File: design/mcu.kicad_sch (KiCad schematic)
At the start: 30 parts, among them J2 SWD_01X04, J3 DEBUG_SPI, U6 STM32H750VBTx, X1 ASTX-H11-25.000MHZ-T

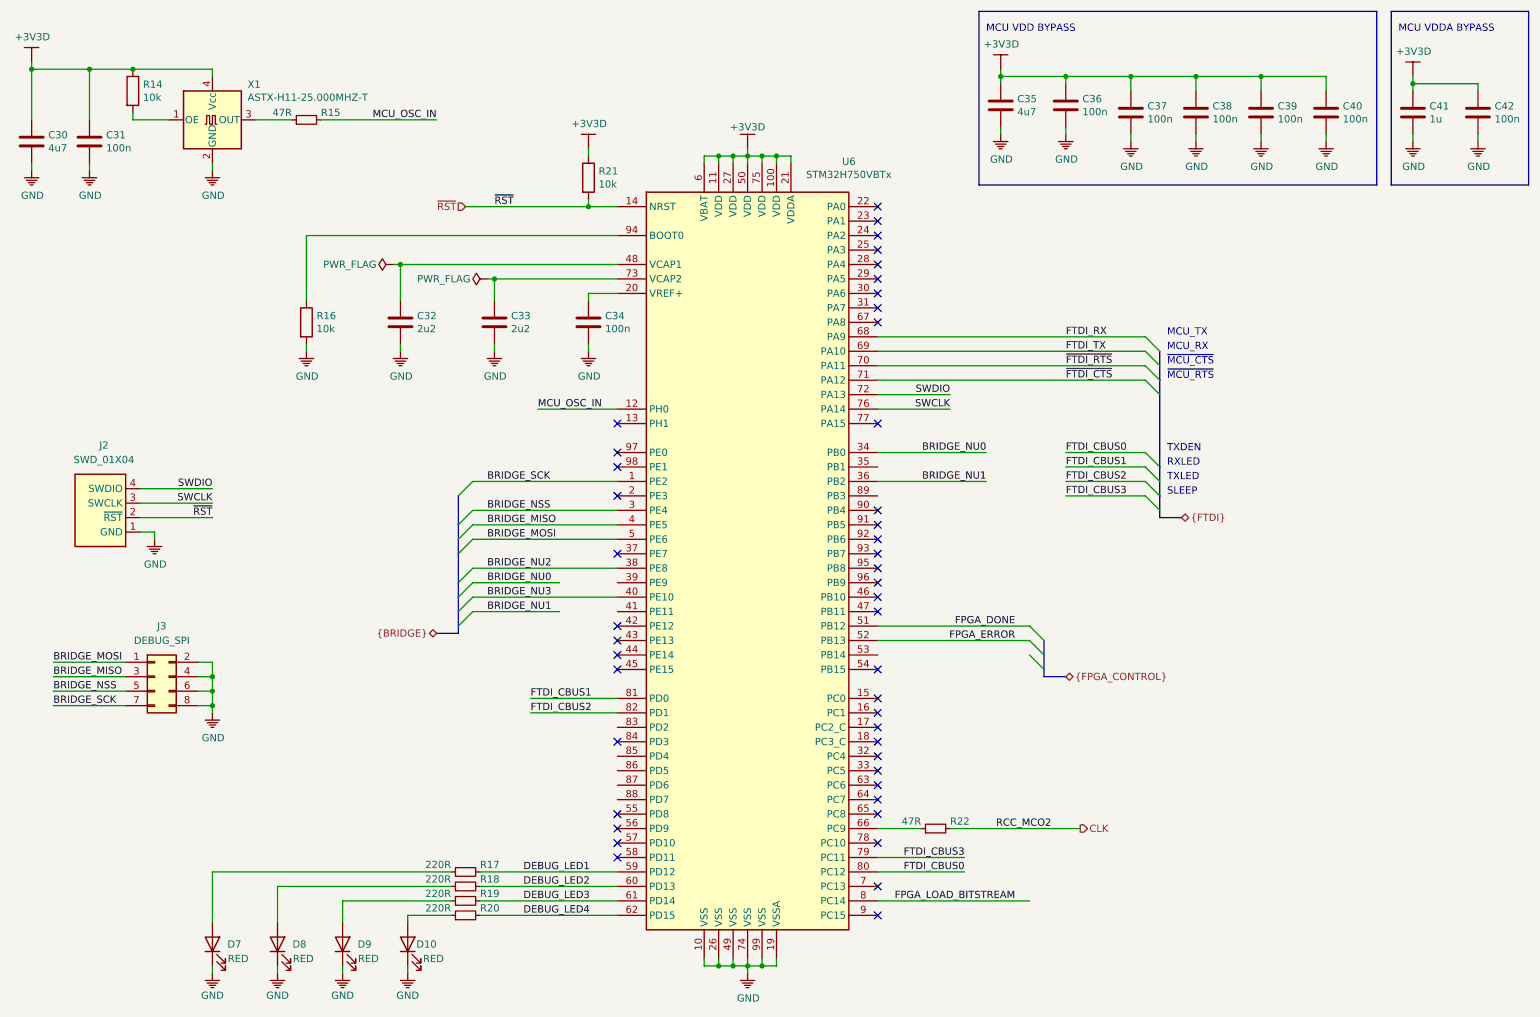
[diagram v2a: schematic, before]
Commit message: Added external oscilator for FPGA and ADC to schematic
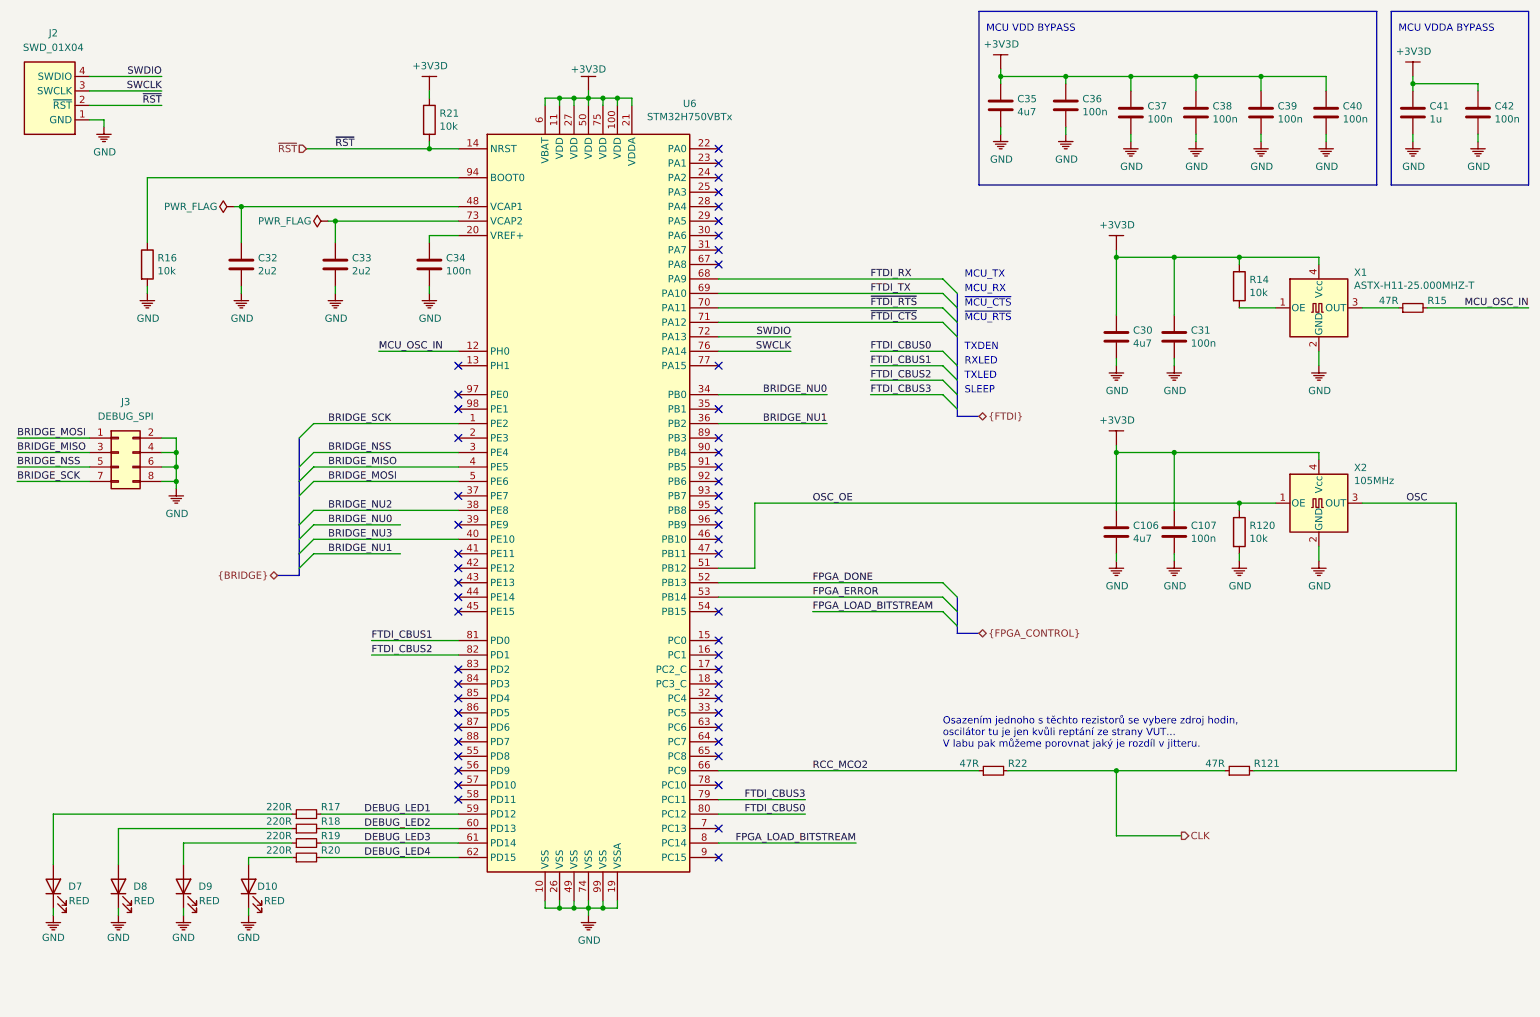
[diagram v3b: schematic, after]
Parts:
- added C106: 4u7, Capacitor_SMD:C_0402_1005Metric, symbol Device:C
- added C107: 100n, Capacitor_SMD:C_0402_1005Metric, symbol Device:C
- added R120: 10k, Resistor_SMD:R_0603_1608Metric, symbol Device:R
- added R121: 47R, Resistor_SMD:R_0402_1005Metric, symbol Device:R_Small
- added X2: 105MHz, Oscillator:Oscillator_SMD_SeikoEpson_SG8002CE-4Pin_3.2x2.5mm, symbol Oscillator:SG-5032CCN
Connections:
- net +3V3D: now also C106.1, C107.1, X2.4 (Vcc)
- net CLK: now also R121.1
- net FPGA_DONE: now also U6.52 (PB13); no longer U6.51 (PB12)
- net FPGA_ERROR: now also U6.53 (PB14); no longer U6.52 (PB13)
- net GND: now also C106.2, C107.2, R120.2, X2.2 (GND)
- net RCC_MCO2: now reaches R22.1, U6.66 (PC9)
- new net OSC: R121.2, X2.3 (OUT)
- new net OSC_OE: R120.1, U6.51 (PB12), X2.1 (OE)
- no-connect marks 45 -> 54
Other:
- note added: "Osazením jednoho s těchto rezistorů se vybere zdroj hodin, oscilátor tu je jen kvůli reptání ze strany VUT... V labu pak můžeme porovnat jaký je rozdíl v jitteru."
- moved on the sheet: C30, C31, C32, C33, C34, D10, D7, D8, D9, J2, J3, R14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

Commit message: Added oscilator layout
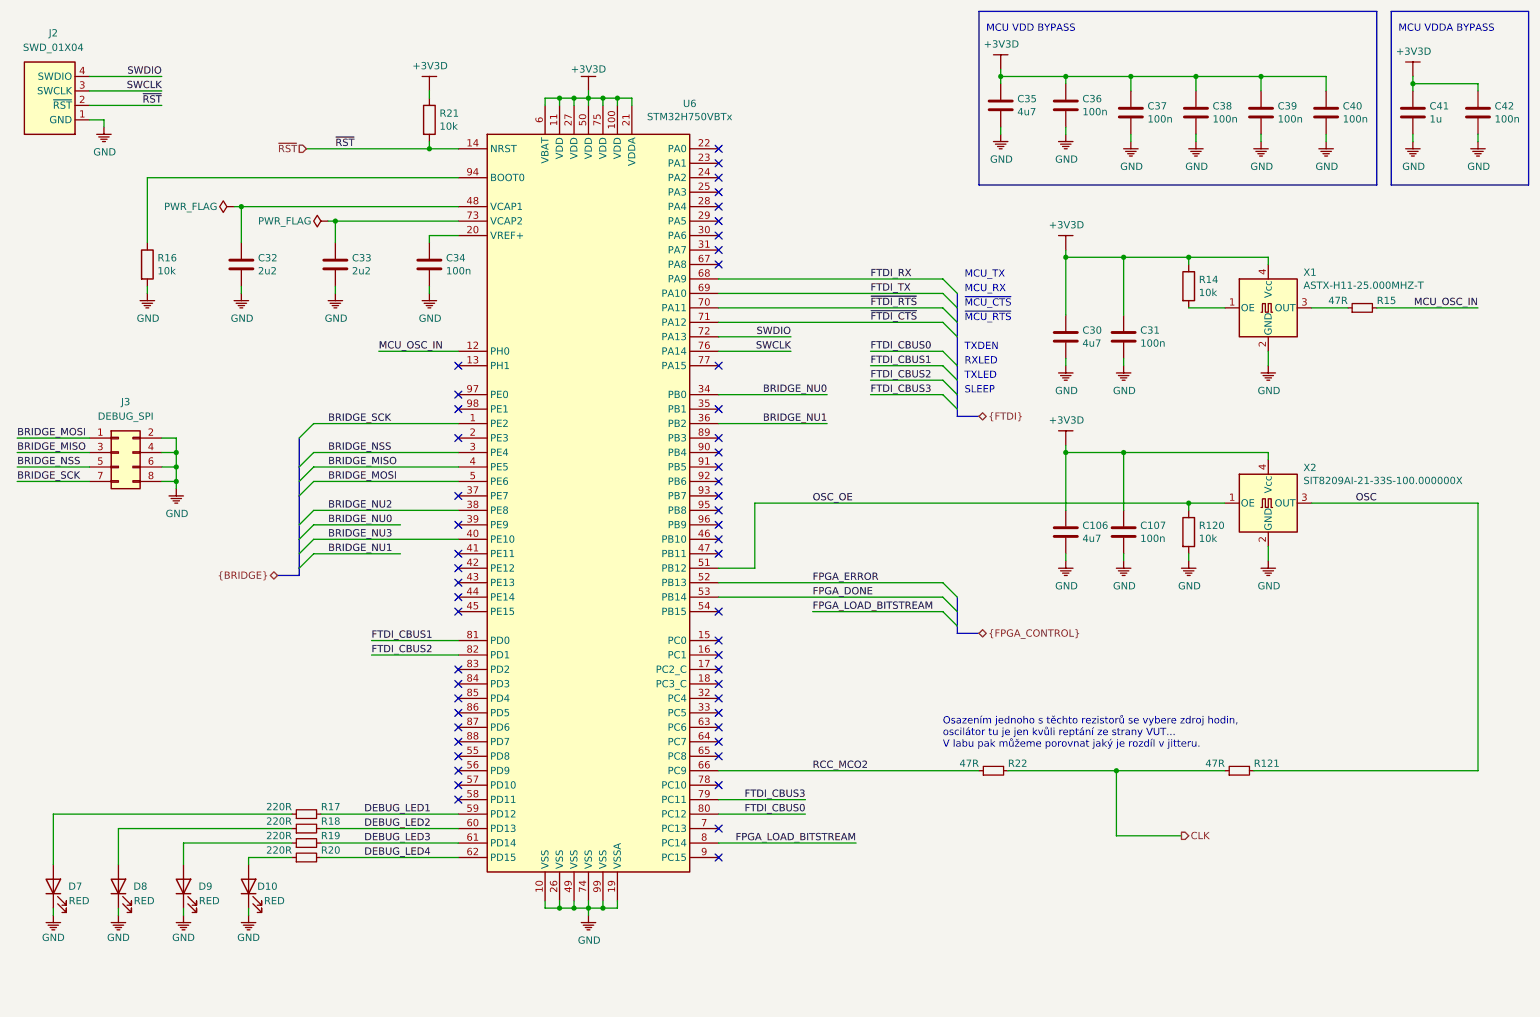
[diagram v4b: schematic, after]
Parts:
- X2: value 105MHz -> SIT8209AI-21-33S-100.000000X
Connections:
- net FPGA_DONE: now also U6.53 (PB14); no longer U6.52 (PB13)
- net FPGA_ERROR: now also U6.52 (PB13); no longer U6.53 (PB14)
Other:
- moved on the sheet: C106, C107, C30, C31, R120, R14, R15, X1, X2

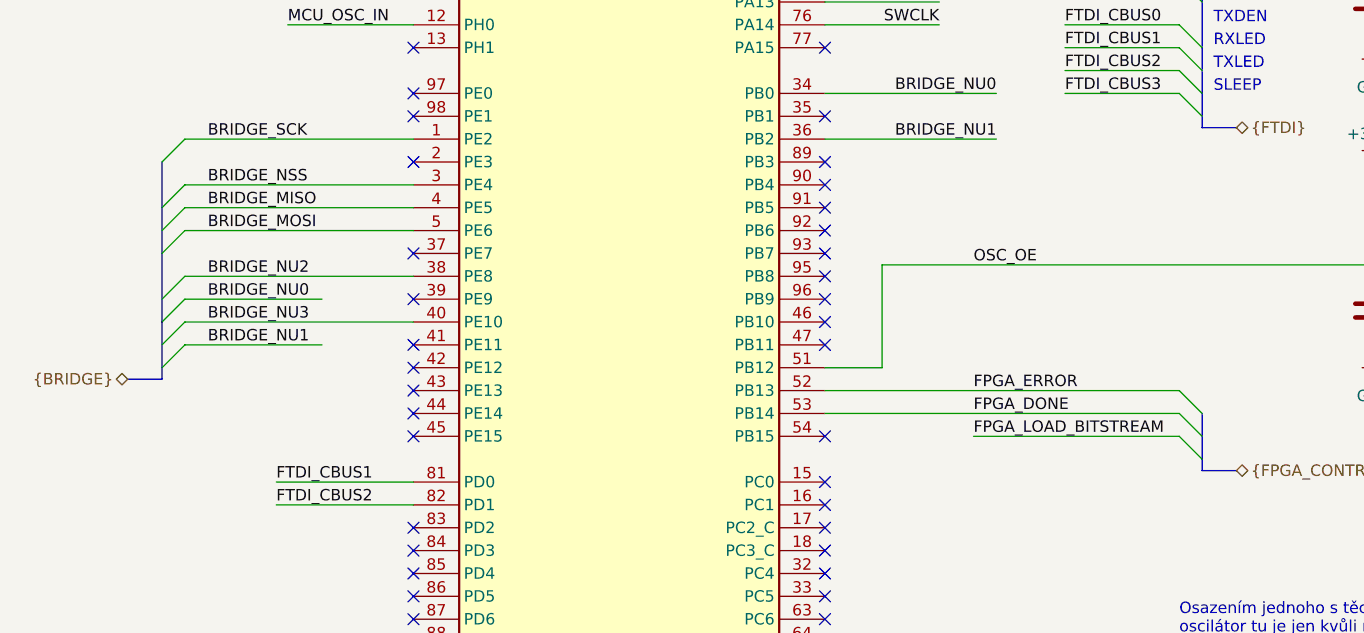
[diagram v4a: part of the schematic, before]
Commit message: Added FTDI RST support
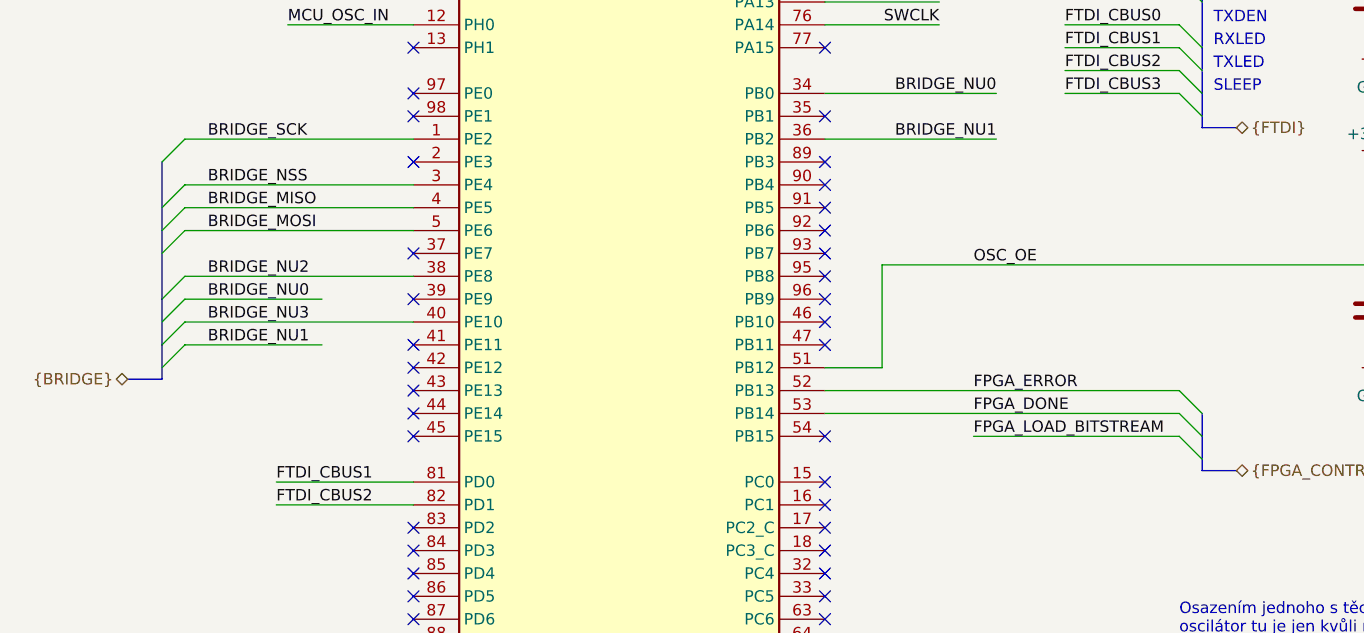
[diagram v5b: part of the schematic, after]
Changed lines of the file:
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@@
-(kicad_sch (version 20200512) (host eeschema "5.99.0-unknown-0658d29~101~ubuntu18.04.1")
+(kicad_sch (version 20200512) (host eeschema "5.99.0-unknown-d72a778~101~ubuntu18.04.1")
   (page 3 8)
   (paper "A4")
@@
   (junction (at 236.22 25.4))
   (junction (at 262.89 26.67))
-  (no_connect (at 95.25 104.14))
-  (no_connect (at 140.97 43.18))
-  (no_connect (at 140.97 96.52))
+  (no_connect (at 140.97 55.88))
+  (no_connect (at 95.25 81.28))
+  (no_connect (at 140.97 83.82))
+  (no_connect (at 95.25 134.62))
+  (no_connect (at 140.97 104.14))
+  (no_connect (at 140.97 99.06))
   (no_connect (at 140.97 157.48))
-  (no_connect (at 140.97 88.9))
-  (no_connect (at 140.97 40.64))
-  (no_connect (at 140.97 38.1))
-  (no_connect (at 95.25 81.28))
-  (no_connect (at 95.25 109.22))
-  (no_connect (at 95.25 134.62))
-  (no_connect (at 95.25 129.54))
-  (no_connect (at 140.97 109.22))
-  (no_connect (at 95.25 119.38))
-  (no_connect (at 95.25 76.2))
-  (no_connect (at 140.97 119.38))
-  (no_connect (at 95.25 99.06))
-  (no_connect (at 140.97 104.14))
-  (no_connect (at 140.97 55.88))
-  (no_connect (at 140.97 139.7))
-  (no_connect (at 140.97 129.54))
-  (no_connect (at 140.97 53.34))
-  (no_connect (at 140.97 99.06))
-  (no_connect (at 95.25 147.32))
-  (no_connect (at 140.97 83.82))
-  (no_connect (at 140.97 58.42))
-  (no_connect (at 140.97 162.56))
-  (no_connect (at 140.97 132.08))
-  (no_connect (at 140.97 149.86))
+  (no_connect (at 95.25 83.82))
+  (no_connect (at 140.97 106.68))
   (no_connect (at 95.25 114.3))
-  (no_connect (at 95.25 144.78))
-  (no_connect (at 95.25 83.82))
-  (no_connect (at 95.25 137.16))
-  (no_connect (at 140.97 134.62))
-  (no_connect (at 140.97 93.98))
-  (no_connect (at 140.97 137.16))
-  (no_connect (at 95.25 149.86))
-  (no_connect (at 140.97 124.46))
-  (no_connect (at 140.97 76.2))
-  (no_connect (at 95.25 88.9))
-  (no_connect (at 95.25 132.08))
-  (no_connect (at 140.97 144.78))
-  (no_connect (at 95.25 142.24))
-  (no_connect (at 140.97 101.6))
-  (no_connect (at 140.97 142.24))
-  (no_connect (at 140.97 50.8))
-  (no_connect (at 140.97 106.68))
-  (no_connect (at 140.97 127))
-  (no_connect (at 140.97 91.44))
-  (no_connect (at 140.97 45.72))
-  (no_connect (at 95.25 116.84))
-  (no_connect (at 95.25 111.76))
-  (no_connect (at 95.25 139.7))
   (no_connect (at 140.97 48.26))
   (no_connect (at 95.25 152.4))
+  (no_connect (at 140.97 119.38))
+  (no_connect (at 140.97 76.2))
+  (no_connect (at 95.25 144.78))
+  (no_connect (at 95.25 104.14))
+  (no_connect (at 95.25 119.38))
+  (no_connect (at 140.97 134.62))
+  (no_connect (at 140.97 53.34))
+  (no_connect (at 140.97 43.18))
+  (no_connect (at 140.97 50.8))
+  (no_connect (at 140.97 88.9))
+  (no_connect (at 95.25 99.06))
+  (no_connect (at 140.97 139.7))
+  (no_connect (at 95.25 116.84))
+  (no_connect (at 140.97 58.42))
+  (no_connect (at 140.97 91.44))
+  (no_connect (at 140.97 144.78))
+  (no_connect (at 95.25 147.32))
+  (no_connect (at 140.97 137.16))
+  (no_connect (at 140.97 149.86))
+  (no_connect (at 140.97 38.1))
+  (no_connect (at 95.25 109.22))
+  (no_connect (at 140.97 93.98))
+  (no_connect (at 95.25 149.86))
+  (no_connect (at 140.97 101.6))
+  (no_connect (at 140.97 109.22))
+  (no_connect (at 140.97 129.54))
+  (no_connect (at 95.25 88.9))
+  (no_connect (at 140.97 142.24))
+  (no_connect (at 95.25 132.08))
+  (no_connect (at 140.97 162.56))
+  (no_connect (at 95.25 76.2))
+  (no_connect (at 95.25 111.76))
+  (no_connect (at 95.25 129.54))
+  (no_connect (at 140.97 40.64))
+  (no_connect (at 140.97 96.52))
+  (no_connect (at 95.25 137.16))
+  (no_connect (at 95.25 142.24))
+  (no_connect (at 140.97 124.46))
+  (no_connect (at 140.97 132.08))
+  (no_connect (at 140.97 45.72))
+  (no_connect (at 95.25 139.7))
+  (no_connect (at 140.97 127))
   (bus_entry (at 67.31 88.9) (size 2.54 -2.54))
   (bus_entry (at 67.31 93.98) (size 2.54 -2.54))
@@
   (wire (pts (xy 274.32 100.33) (xy 274.32 147.32)))
   (bus (pts (xy 63.5 113.03) (xy 67.31 113.03)))
-  (bus (pts (xy 67.31 88.9) (xy 67.31 93.98)))
-  (bus (pts (xy 67.31 93.98) (xy 67.31 99.06)))
-  (bus (pts (xy 67.31 99.06) (xy 67.31 106.68)))
-  (bus (pts (xy 67.31 106.68) (xy 67.31 111.76)))
-  (bus (pts (xy 67.31 111.76) (xy 67.31 113.03)))
+  (bus (pts (xy 67.31 88.9) (xy 67.31 96.52)))
+  (bus (pts (xy 67.31 96.52) (xy 67.31 104.14)))
+  (bus (pts (xy 67.31 104.14) (xy 67.31 109.22)))
+  (bus (pts (xy 67.31 109.22) (xy 67.31 113.03)))
   (bus (pts (xy 182.88 63.5) (xy 182.88 68.58)))
   (bus (pts (xy 182.88 68.58) (xy 182.88 76.2)))
@@
   (bus (pts (xy 182.88 81.28) (xy 182.88 85.09)))
   (bus (pts (xy 182.88 85.09) (xy 186.69 85.09)))
-  (bus (pts (xy 182.88 116.84) (xy 182.88 121.92)))
-  (bus (pts (xy 182.88 121.92) (xy 182.88 123.19)))
+  (bus (pts (xy 182.88 116.84) (xy 182.88 119.38)))
+  (bus (pts (xy 182.88 119.38) (xy 182.88 123.19)))
   (bus (pts (xy 186.69 123.19) (xy 182.88 123.19)))
   (polyline (pts (xy 186.69 13.97) (xy 186.69 44.45)))
